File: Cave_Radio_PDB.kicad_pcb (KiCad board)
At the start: 2 copper layers, 76.5 x 50 mm, 77 parts, among them J1 JST_PH_01x06, J2 Conn_01x02, J3 Conn_01x02, J4 Conn_01x02, J5 USB_A, J6 Conn_01x02, J7 Barrel_Jack, J8 Conn_01x02, U1 TPS25751D, U2 CAT24C256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

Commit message: Update footprints
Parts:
- removed J1: JST_PH_01x06, Cave_Radio_PDB:CONN6_S6B-PH_JST
- added C31: 10uF, Cave_Radio_PDB:R_0603_1608Metric, F.Cu at (7.67, 0.48)
- added C32: 1nF, Cave_Radio_PDB:C_0402_1005Metric, F.Cu at (194.5, 52.8)
- added C33: 1nF, Cave_Radio_PDB:C_0402_1005Metric, F.Cu at (194.5, 54.9)
- added J9: USB4110GFA, Cave_Radio_PDB:GCT_USB4110GFA, F.Cu at (184.0, 54.7)
- added R24: 0, Cave_Radio_PDB:R_0402_1005Metric, F.Cu at (0.95, 11.7)
- added R25: 0, Cave_Radio_PDB:R_0402_1005Metric, F.Cu at (0.95, 13.7)
- added R26: 0, Cave_Radio_PDB:R_0402_1005Metric, F.Cu at (0.95, 15.7)
- added U9: NSR0340HT1G, Cave_Radio_PDB:SOD-323_1P8X1P35_ONS, F.Cu at (2.03, 6.21)
- C10, C9: value 220pF -> 1nF
- C11, C12, C5, C6, C7, C8: footprint Cave_Radio_PDB:C_0402_1005Metric -> Cave_Radio_PDB:R_0603_1608Metric
- C4: value 0.1uF -> 10uF; footprint Cave_Radio_PDB:C_0402_1005Metric -> Cave_Radio_PDB:R_0603_1608Metric
- J5: value USB_A -> Conn_01x03; footprint Cave_Radio_PDB:CINCH_SS-52100-001 -> Cave_Radio_PDB:CONN_TSW-103-S_SAI
- J7: value Barrel_Jack -> Conn_01x02; footprint Cave_Radio_PDB:CUI_PJ-102A -> Cave_Radio_PDB:CONN_TSW-102-S_SAI
- R7: value 0 -> 10k
- R9: value 10k -> 1.65k
- U1: footprint Package_DFN_QFN:Texas_REF0038A_WQFN-38-2EP_6x4mm_P0.4 -> Cave_Radio_PDB:Texas_REF0038A_WQFN-38-2EP_6x4mm_P0.4
- U3, U4: footprint Package_SON:WSON-6-1EP_2x2mm_P0.65mm_EP1x1.6mm -> Cave_Radio_PDB:WSON-6-1EP_2x2mm_P0.65mm_EP1x1.6mm_ThermalVias
- U5: footprint Package_TO_SOT_SMD:SOT-553 -> Cave_Radio_PDB:SOT-553
- U8: footprint Package_SON:VSON-10-1EP_3x3mm_P0.5mm_EP1.65x2.4mm_ThermalVias -> Cave_Radio_PDB:VSON-10-1EP_3x3mm_P0.5mm_EP1.65x2.4mm_ThermalVias
- moved C4 212.3 mm to (3.85, 11.7)
- moved R7 208.8 mm to (6.01, 5.71)
- moved R8 208.8 mm to (6.01, 7.70)
- moved J7 181.6 mm to (1.60, 1.60), turned to 0 degrees
- moved J5 29.2 mm to (179.1, 63.8), turned to 0 degrees
- moved C9 23.6 mm to (187.6, 62.8)
- moved C10 23.5 mm to (187.6, 64.9)
- moved R9 16.1 mm to (194.5, 57.0)
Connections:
- J5 pad 1: Net-(J5-VBUS) -> /USB/D+
- J5 pad 3: /USB/D+ -> GND
- R7 pad 1: Net-(J5-Shield) -> Net-(U8-IN)
- R7 pad 2: GND -> Net-(U8-OVCSEL)
- R8 pad 1: VBUS -> Net-(U8-OVCSEL)
- R8 pad 2: Net-(J5-VBUS) -> GND
- R9 pad 1: GND -> Net-(U8-ILM)
- R9 pad 2: Net-(J5-VBUS) -> GND
- U5 pad 3: /USB/D- -> /USB/D+
- U5 pad 5: /USB/D+ -> /USB/D-
- U8 pad 10: unconnected-(U8-ITIMER-Pad10) -> Net-(U8-ITIMER)
- U8 pad 2: unconnected-(U8-OVCSEL-Pad2) -> Net-(U8-OVCSEL)
- U8 pad 3: unconnected-(U8-PG-Pad3) -> GND
- U8 pad 4: unconnected-(U8-PGTH-Pad4) -> GND
- U8 pad 7: unconnected-(U8-DVDT-Pad7) -> Net-(U8-DVDT)
- U8 pad 8: unconnected-(U8-GND-Pad8) -> GND
- U8 pad 9: unconnected-(U8-ILM-Pad9) -> Net-(U8-ILM)

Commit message: start layout
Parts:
- removed C5, C8: 10uF, Cave_Radio_PDB:R_0603_1608Metric
- removed J2, J3, J4: Conn_01x02, Cave_Radio_PDB:CONN_TSW-102-S_SAI
- added H7: Zip_Tie_Support, Cave_Radio_PDB:Zip_Tie_Support, F.Cu at (141.5, 71.5)
- added H8: Zip_Tie_Support, Cave_Radio_PDB:Zip_Tie_Support, F.Cu at (141.5, 84.8)
- added J1: Conn_01x02, Cave_Radio_PDB:CONN_102_PWR, F.Cu at (107.2, 64.0)
- added TP1: TP_01, Cave_Radio_PDB:CONN_TP, F.Cu at (131.0, 86.8)
- added TP2: TP_01, Cave_Radio_PDB:CONN_TP, F.Cu at (128.5, 86.8)
- added TP3: TP_01, Cave_Radio_PDB:CONN_TP, F.Cu at (126.0, 86.8)
- H5, H6: value MountingHole_Pad -> Zip_Tie_Support; footprint Cave_Radio_PDB:MountingHole_3.2mm_M3_DIN965_Pad_TopBottom -> Cave_Radio_PDB:Zip_Tie_Support
- U2: footprint Cave_Radio_PDB:SOIC-8_5.3x5.3mm_P1.27mm -> Cave_Radio_PDB:UDFN8_2X3_ONS
- U8: footprint Cave_Radio_PDB:VSON-10-1EP_3x3mm_P0.5mm_EP1.65x2.4mm_ThermalVias -> Cave_Radio_PDB:VQFN8_PWR_TEX
- moved J7 153.9 mm to (133.8, 80.5), turned to -90 degrees
- moved R24 149.2 mm to (131.0, 84.8), turned to 90 degrees
- moved R26 145.1 mm to (128.5, 84.8), turned to 90 degrees
- moved R25 143.8 mm to (126.0, 84.8), turned to 90 degrees
- moved C4 135.9 mm to (125.8, 71.6), turned to 180 degrees
- moved R23 118.2 mm to (95.3, 68.6), turned to 90 degrees
- moved U9 114.8 mm to (95.8, 72.5)
- moved C18 112.7 mm to (99.6, 83.2), turned to -90 degrees
- moved R22 112.5 mm to (99.6, 85.2), turned to 90 degrees
- moved C31 112.2 mm to (98.9, 65.8), turned to 90 degrees
- moved R21 111.5 mm to (100.6, 83.2), turned to 90 degrees
- moved C14 111.2 mm to (99.6, 70.2), turned to -90 degrees
- moved R7 110.0 mm to (96.3, 68.6), turned to 90 degrees
- moved R8 109.7 mm to (97.2, 68.6), turned to -90 degrees
- moved R20 108.6 mm to (100.6, 85.2), turned to 90 degrees
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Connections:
- C1 pad 1: LDO_3V3 -> 3V3_EEPROM
- C11 pad 1: Net-(J4-Pin_2) -> LDO_3V3
- C31 pad 1: Net-(U8-IN) -> Net-(J1-Pin_2)
- J6 pad 2: GND -> LDO_3V3
- J7 pad 1: 9V -> GND
- J7 pad 2: GND -> 9V
- J8 pad 1: Net-(J8-Pin_1) -> Net-(J1-Pin_2)
- J8 pad 2: GND -> Net-(J8-Pin_2)
- R14 pad 1: LDO_3V3 -> /USB/PD_EN
- R14 pad 2: /USB/PD_EN -> GND
- R23 pad 1: Net-(U8-IN) -> GND
- R23 pad 2: Net-(J8-Pin_1) -> Net-(J8-Pin_2)
- R24 pad 1: LDO_3V3 -> 3V3_EEPROM
- R24 pad 2: Net-(J4-Pin_2) -> LDO_3V3
- R5 pad 1: LDO_3V3 -> 3V3_EEPROM
- R6 pad 1: LDO_3V3 -> 3V3_EEPROM
- R7 pad 1: Net-(U8-IN) -> Net-(J1-Pin_2)
- U1 pad 1: Net-(J4-Pin_2) -> LDO_3V3
- U2 pad 8: LDO_3V3 -> 3V3_EEPROM
- U6 pad 7: (no net) -> Net-(U6-FB)
- U7 pad 7: (no net) -> Net-(U7-FB)
- U8 pad 1: Net-(J8-Pin_1) -> Net-(J8-Pin_2)
- U8 pad 5: Net-(U8-IN) -> Net-(J1-Pin_2)
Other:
- board size 76.5 x 50 mm -> 53 x 37.8 mm

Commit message: initial layout
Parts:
- moved C9 2.44 mm to (130.2, 74.0), turned to 0 degrees
- moved R22 2.00 mm to (99.6, 83.2), turned to -90 degrees
- moved R17 2.00 mm to (99.6, 70.2), turned to -90 degrees
- moved R15 2.00 mm to (100.6, 70.2), turned to -90 degrees
- moved R16 2.00 mm to (100.6, 72.2), turned to -90 degrees
- moved R20 2.00 mm to (100.6, 83.2), turned to -90 degrees
- moved R21 2.00 mm to (100.6, 85.2), turned to -90 degrees
- moved C14 2.00 mm to (99.6, 72.2), turned to 90 degrees
- moved C18 1.97 mm to (99.6, 85.2), turned to 90 degrees
- moved R6 1.46 mm to (131.5, 79.2)
- moved H8 1.32 mm to (140.2, 84.5)
- moved C11 1.31 mm to (121.3, 77.0)
- moved R10 1.31 mm to (121.9, 79.5)
- moved R11 1.31 mm to (121.9, 78.5)
- moved R12 1.31 mm to (121.9, 80.5)
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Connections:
- J5 pad 1: /USB/D+ -> GND
- J5 pad 2: /USB/D- -> /USB/D+
- J5 pad 3: GND -> /USB/D-
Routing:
- net GND: track 0.00 -> 60.7 mm, vias 0 -> 60
- net LDO_3V3: track 0.00 -> 34.5 mm, vias 0 -> 4
- net Net-(J1-Pin_2): track 0.00 -> 28.6 mm, vias 0 -> 1
- net Net-(J8-Pin_2): track 0.00 -> 19.2 mm, vias 0 -> 2
- net 3V3_EEPROM: track 0.00 -> 17.1 mm, vias 0 -> 2
- net /USB/PD_EN: track 0.00 -> 16.9 mm, vias 0 -> 2
- net Net-(TP3-Pin_1): track 0.00 -> 16.1 mm, vias 0 -> 1
- net /USB/CC2: track 0.00 -> 14.8 mm
- net /USB/CC1: track 0.00 -> 14.1 mm, vias 0 -> 2
- net /USB/D+: track 0.00 -> 13.3 mm
- net Net-(TP2-Pin_1): track 0.00 -> 13.0 mm
- net 9V: track 0.00 -> 12.8 mm, vias 0 -> 2
- net 5V: track 0.00 -> 11.0 mm, vias 0 -> 2
- net /USB/D-: track 0.00 -> 9.84 mm
- net 3V3: track 0.00 -> 9.40 mm, vias 0 -> 2
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- added copper zone on F.Cu, net 5V
- added copper zone on F.Cu, net 9V
- added copper zone on B.Cu, net GND
- added copper zone on F.Cu, net GND
- added copper zone on F.Cu, net Net-(C13-Pad1)
- added copper zone on F.Cu, net Net-(C17-Pad1)
- added copper zone on F.Cu, net Net-(J1-Pin_2)
- added copper zone on F.Cu, net VBATT
- added copper zone on B.Cu, net VBUS
- added copper zone on F.Cu, net VBUS
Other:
- board size 53 x 37.8 mm -> 52 x 37.5 mm
- board text added: "+"
- board text added: "-"
- board text added: "9V"
- board text added: "BATTERY"
- board text added: "Cave Radio PDB V1 Evan Peters VE7ITX March 2026"
- board text added: "D+"
- board text added: "D-"
- board text added: "GND"
- board text added: "PHN_EN"
- board text added: "PWR_EN"
- board text added: "R_DATA"
- board text added: "R_PWR"

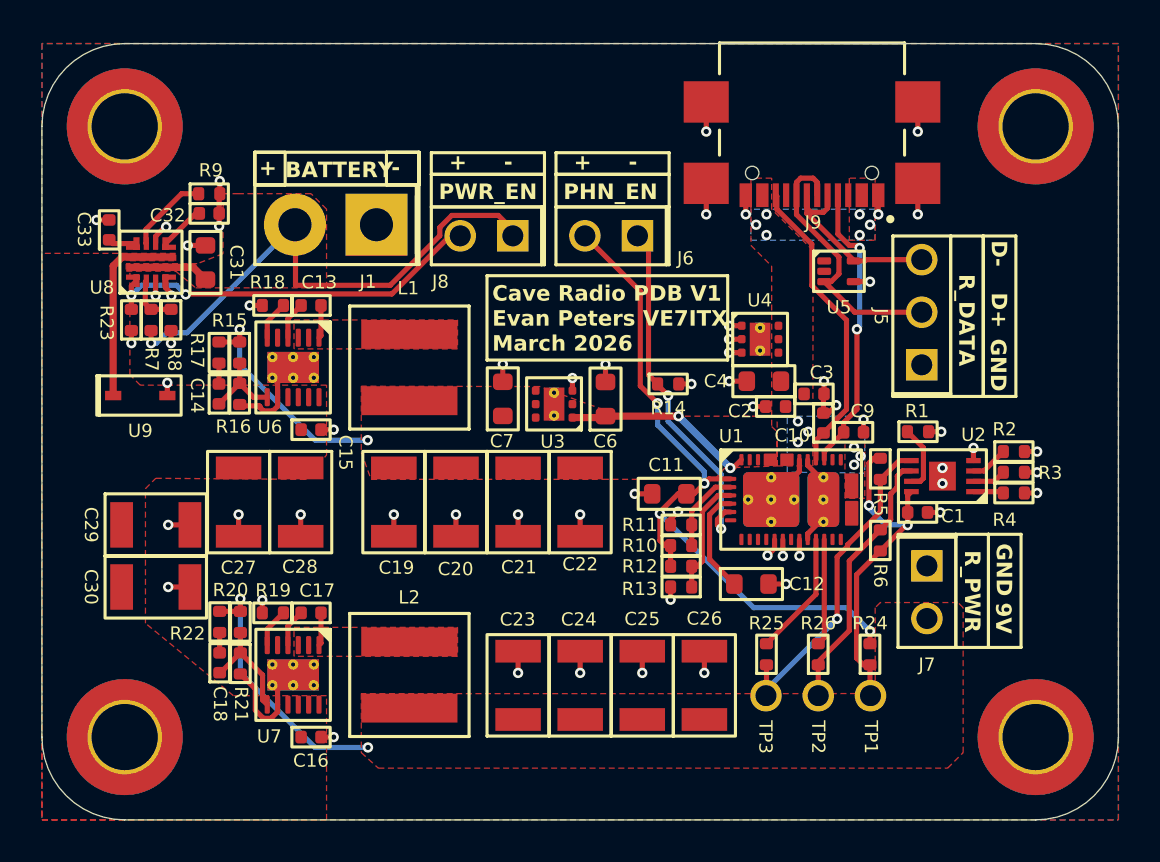
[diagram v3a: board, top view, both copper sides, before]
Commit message: add via stitching
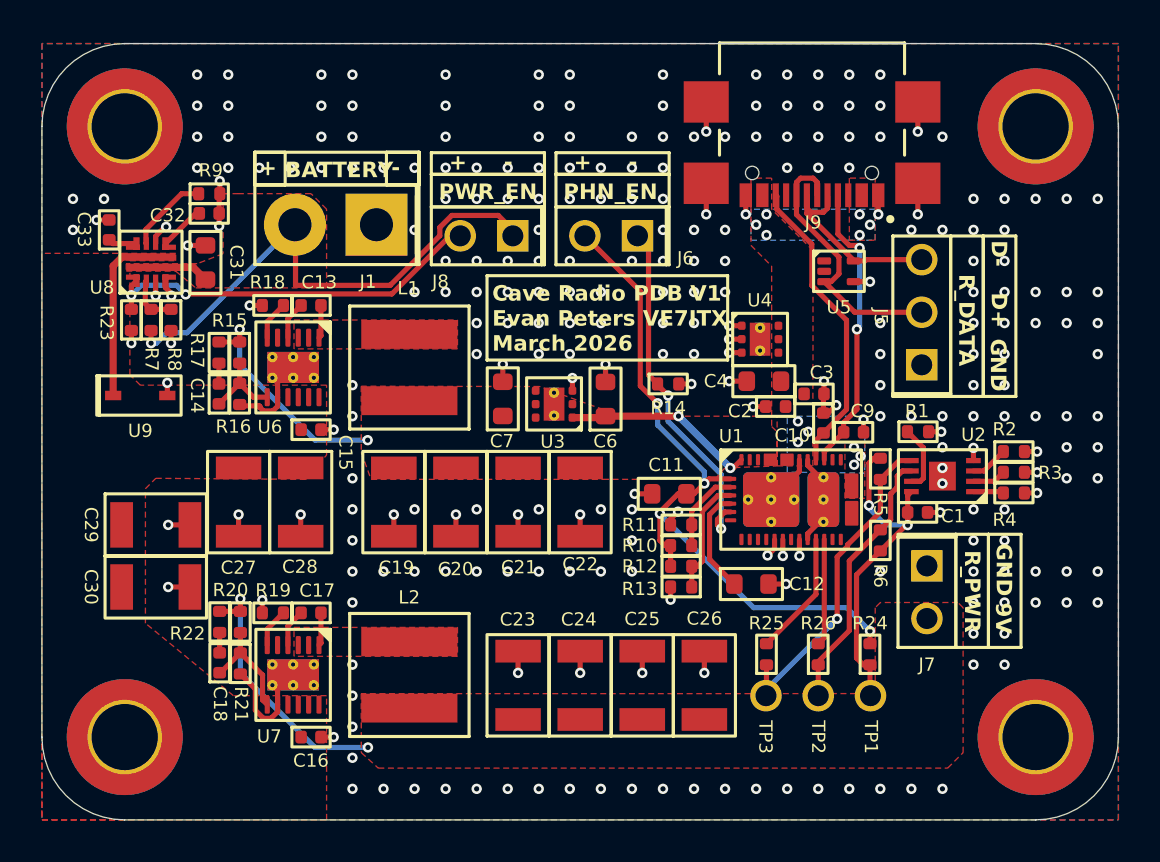
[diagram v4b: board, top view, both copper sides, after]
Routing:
- net GND: vias 60 -> 276
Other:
- board text added: "{ "ViaStitching": "0.2", "stitch_zone_0": { "HSpacing": "1.5", "VSpacing": "1.5", "HOffset": "0", "VOffset": "0", "Clearance": "0", "Randomize": false } }"
- board text added: "{ "ViaStitching": "0.2", "stitch_zone_0": { "HSpacing": "2", "VSpacing": "2", "HOffset": "0", "VOffset": "1", "Clearance": "0", "Randomize": false } }"
- board text added: "{ "ViaStitching": "0.2", "stitch_zone_0": { "HSpacing": "3", "VSpacing": "3", "HOffset": "0", "VOffset": "1.5", "Clearance": "0", "Randomize": false } }"

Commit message: remove efuse, add led connectors
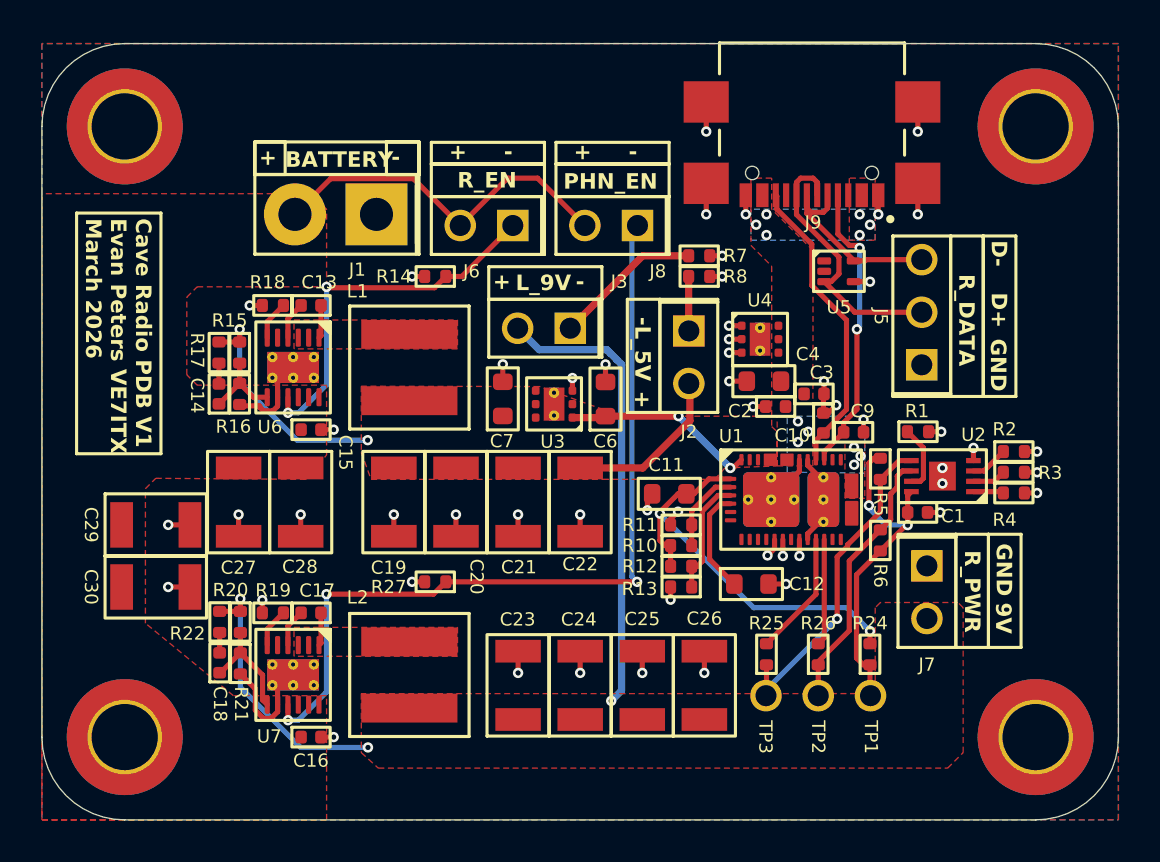
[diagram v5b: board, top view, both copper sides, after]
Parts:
- removed C31: 10uF, Cave_Radio_PDB:R_0603_1608Metric
- removed C32, C33: 1nF, Cave_Radio_PDB:C_0402_1005Metric
- removed R23: 10k, Cave_Radio_PDB:R_0402_1005Metric
- removed R9: 1.65k, Cave_Radio_PDB:R_0402_1005Metric
- removed U8: TPS259472LRPWR, Cave_Radio_PDB:VQFN8_PWR_TEX
- removed U9: NSR0340HT1G, Cave_Radio_PDB:SOD-323_1P8X1P35_ONS
- added J2: Conn_01x02, Cave_Radio_PDB:CONN_TSW-102-S_SAI, F.Cu at (122.2, 69.1)
- added J3: Conn_01x02, Cave_Radio_PDB:CONN_TSW-102-S_SAI, F.Cu at (116.5, 69.0)
- added R27: 10k, Cave_Radio_PDB:R_0402_1005Metric, F.Cu at (110.0, 81.2)
- R7, R8: value 10k -> 0
- moved R7 26.7 mm to (122.8, 65.5), turned to 180 degrees
- moved R8 25.6 mm to (122.8, 66.5), turned to 180 degrees
- moved R14 12.4 mm to (110.0, 66.5), turned to 180 degrees
- moved J6 6.04 mm to (113.7, 64.0)
- moved J8 6.04 mm to (119.8, 64.0)
- moved J1 0.50 mm to (107.2, 63.5)
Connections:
- J1 pad 2: Net-(J1-Pin_2) -> VBATT
- J6 pad 1: /USB/PD_EN -> /Power/5V_EN
- J6 pad 2: LDO_3V3 -> VBATT
- J8 pad 1: Net-(J1-Pin_2) -> /Power/9V_EN
- J8 pad 2: Net-(J8-Pin_2) -> VBATT
- R14 pad 1: /USB/PD_EN -> /Power/5V_EN
- R7 pad 1: Net-(J1-Pin_2) -> GND
- R7 pad 2: Net-(U8-OVCSEL) -> Net-(J3-Pin_1)
- R8 pad 1: Net-(U8-OVCSEL) -> GND
- R8 pad 2: GND -> Net-(J2-Pin_1)
- U1 pad 5: /USB/PD_EN -> unconnected-(U1-GPIO0-Pad5)
- U6 pad 9: VBATT -> /Power/5V_EN
- U7 pad 9: VBATT -> /Power/9V_EN
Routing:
- net /Power/9V_EN: track 0.00 -> 40.6 mm, vias 0 -> 3
- net Net-(J1-Pin_2): track 28.6 -> 0.00 mm, vias 1 -> 0
- net 9V: track 12.8 -> 35.5 mm, vias 2 -> 3
- net Net-(J8-Pin_2): track 19.2 -> 0.00 mm, vias 2 -> 0
- net /Power/5V_EN: track 0.00 -> 18.2 mm, vias 0 -> 2
- net /USB/PD_EN: track 16.9 -> 0.00 mm, vias 2 -> 0
- net LDO_3V3: track 34.5 -> 20.2 mm, vias 4 -> 2
- net VBATT: track 8.26 -> 17.6 mm
- net 5V: track 11.0 -> 19.6 mm
- net Net-(J3-Pin_1): track 0.00 -> 7.17 mm
- net GND: track 60.7 -> 54.7 mm, vias 276 -> 53
- net Net-(U8-ILM): track 3.95 -> 0.00 mm
- net Net-(J2-Pin_1): track 0.00 -> 2.64 mm
- net Net-(U8-OVCSEL): track 2.48 -> 0.00 mm
- net Net-(U8-DVDT): track 2.24 -> 0.00 mm
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- removed copper zone on F.Cu, net Net-(J1-Pin_2)
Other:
- board text added: "L_5V"
- board text added: "L_9V"
- board text added: "R_EN"
- board text removed: "PWR_EN"

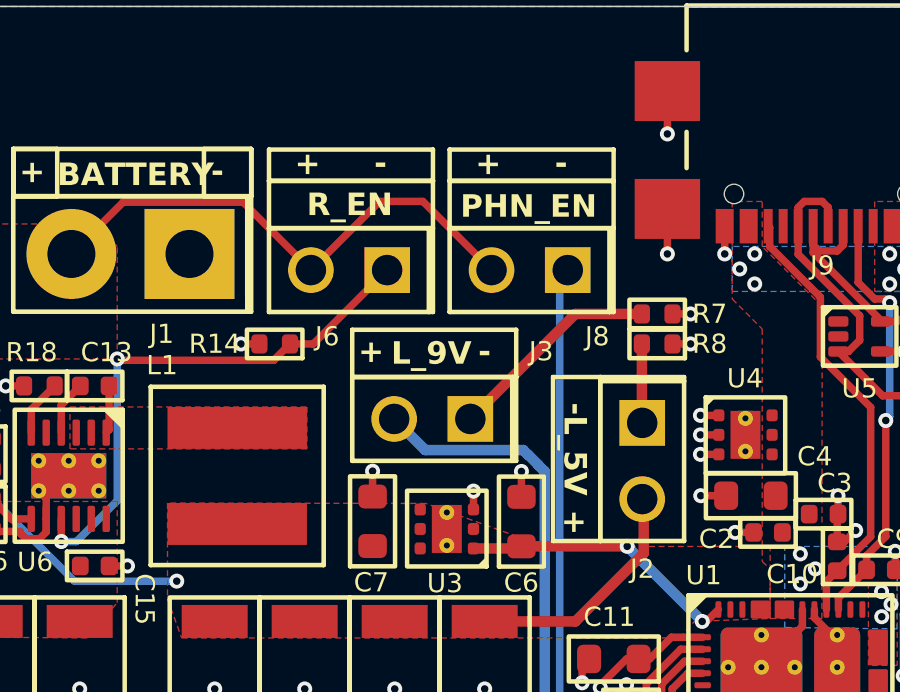
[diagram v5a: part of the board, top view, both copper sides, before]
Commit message: add bom
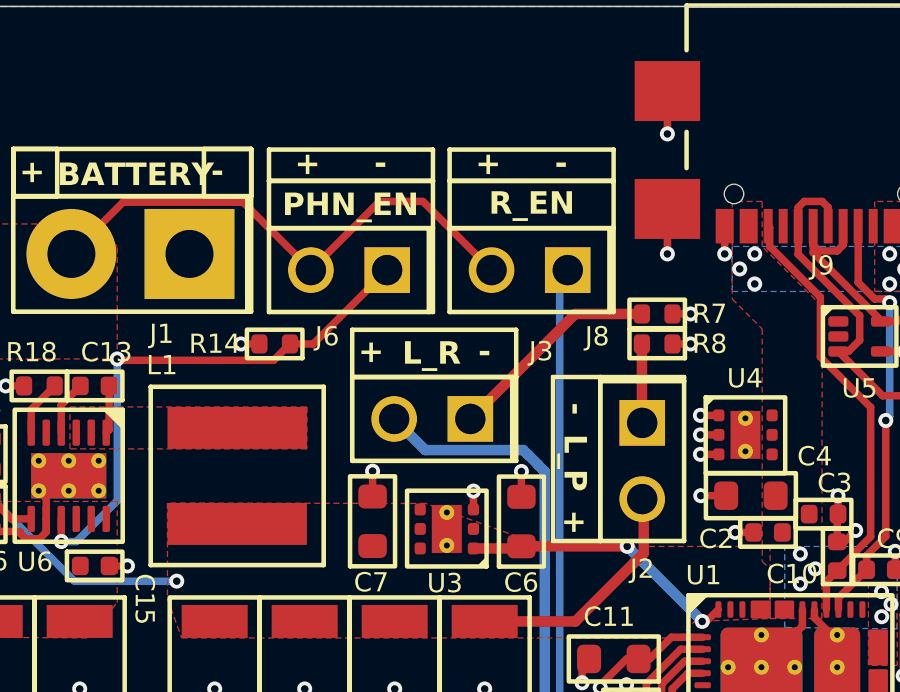
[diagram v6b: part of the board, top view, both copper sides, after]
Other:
- board text added: "L_P"
- board text added: "L_R"
- board text removed: "L_5V"
- board text removed: "L_9V"
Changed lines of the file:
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@@
 		)
 	)
-	(gr_text "+"
-		(at 110.665615 60.928943 0)
+	(gr_text "PHN_EN"
+		(at 110.25 62.295356 0)
 		(layer "F.SilkS")
 		(effects
@@
 		)
 	)
-	(gr_text "R_EN"
-		(at 111.067014 62.295356 0)
+	(gr_text "+"
+		(at 110.665615 60.928943 0)
 		(layer "F.SilkS")
 		(effects
@@
 		)
 	)
-	(gr_text "L_9V"
-		(at 113.881773 67.25 0)
-		(layer "F.SilkS")
-		(effects
-			(font
-				(size 0.75 0.75)
-				(thickness 0.1875)
-				(bold yes)
-			)
-			(justify left bottom)
-		)
-	)
-	(gr_text "PHN_EN"
-		(at 116.186896 62.350591 0)
+	(gr_text "L_R"
+		(at 114.25 67.25 0)
 		(layer "F.SilkS")
 		(effects
@@
 	(gr_text "-"
 		(at 116.781791 67.191864 0)
+		(layer "F.SilkS")
+		(effects
+			(font
+				(size 0.75 0.75)
+				(thickness 0.1875)
+				(bold yes)
+			)
+			(justify left bottom)
+		)
+	)
+	(gr_text "R_EN"
+		(at 117.134348 62.25 0)
 		(layer "F.SilkS")
 		(effects
@@
 		)
 	)
-	(gr_text "L_5V"
-		(at 119.569399 68.876364 270)
+	(gr_text "L_P"
+		(at 119.569399 69.5 270)
 		(layer "F.SilkS")
 		(effects
